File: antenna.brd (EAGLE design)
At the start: 98 x 98 mm, 4 parts, among them X1 BU-SMA-V

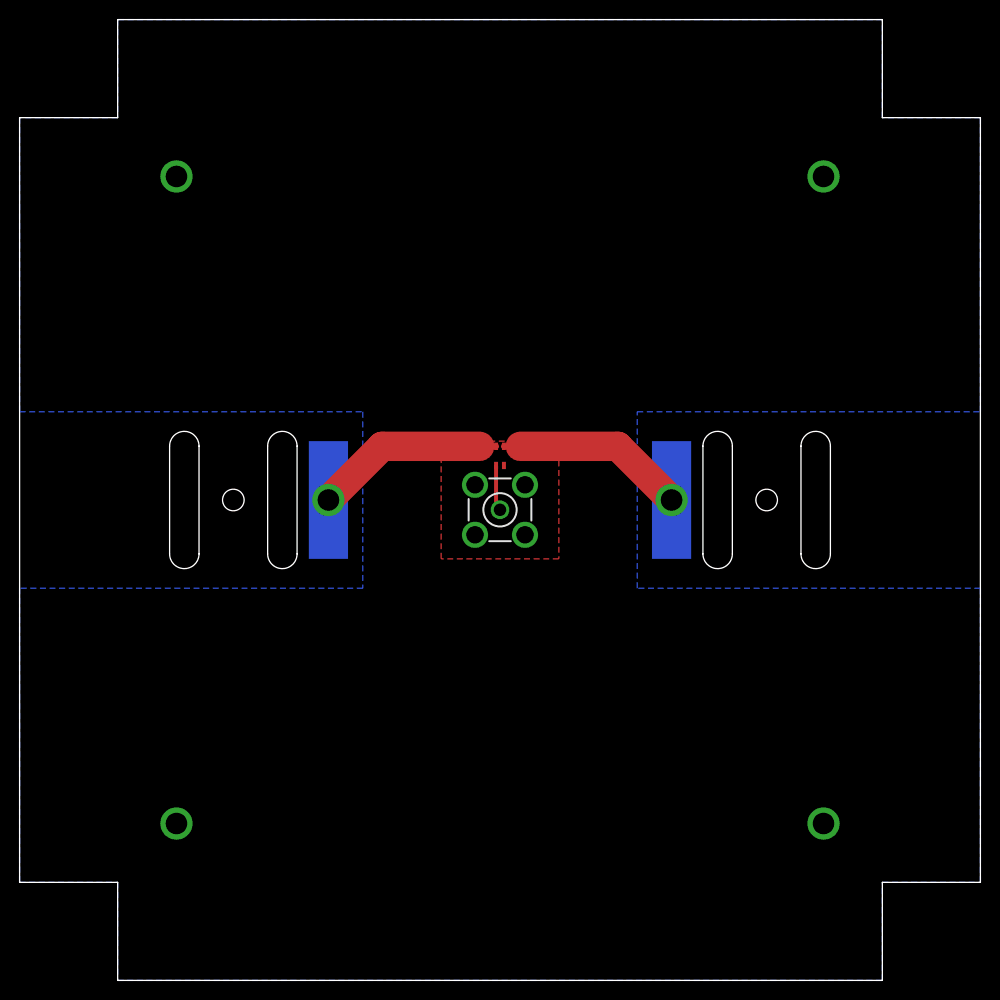
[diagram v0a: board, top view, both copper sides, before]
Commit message: Tweaks to antenna board
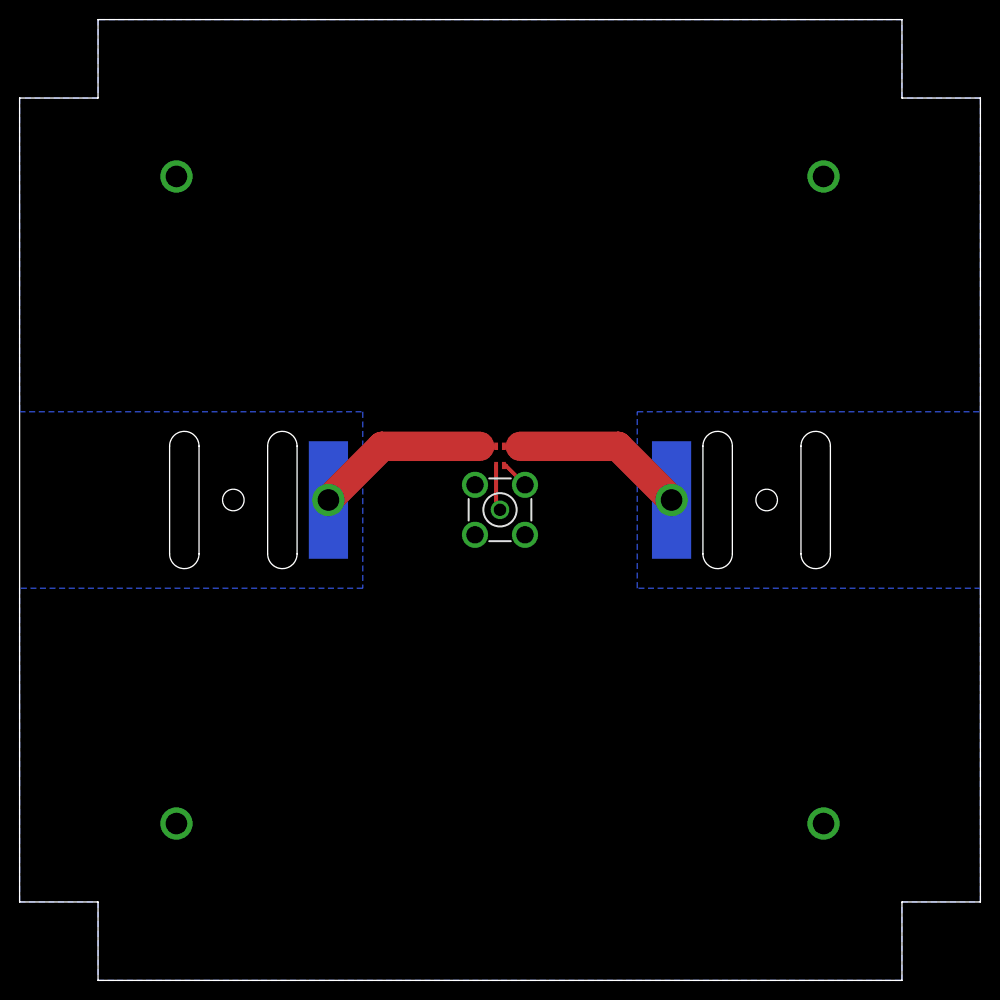
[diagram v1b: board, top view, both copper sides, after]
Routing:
- net GND: track 0.00 -> 2.97 mm
- removed copper zone on layer 1, net GND
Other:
- outline, holes or cut-outs redrawn
- board text added: "Antenna Board V1.1"
- board text removed: "Antenna Board V1.0"
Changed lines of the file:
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@@
 <board>
 <plain>
-<wire x1="0" y1="10" x2="10" y2="10" width="0" layer="20"/>
-<wire x1="10" y1="10" x2="10" y2="0" width="0" layer="20"/>
-<wire x1="10" y1="0" x2="88" y2="0" width="0" layer="20"/>
-<wire x1="88" y1="0" x2="88" y2="10" width="0" layer="20"/>
-<wire x1="88" y1="10" x2="98" y2="10" width="0" layer="20"/>
-<wire x1="98" y1="10" x2="98" y2="88" width="0" layer="20"/>
-<wire x1="98" y1="88" x2="88" y2="88" width="0" layer="20"/>
-<wire x1="88" y1="88" x2="88" y2="98" width="0" layer="20"/>
-<wire x1="88" y1="98" x2="10" y2="98" width="0" layer="20"/>
-<wire x1="10" y1="98" x2="10" y2="88" width="0" layer="20"/>
-<wire x1="10" y1="88" x2="0" y2="88" width="0" layer="20"/>
-<wire x1="0" y1="88" x2="0" y2="10" width="0" layer="20"/>
+<wire x1="0" y1="8" x2="8" y2="8" width="0" layer="20"/>
+<wire x1="8" y1="8" x2="8" y2="0" width="0" layer="20"/>
+<wire x1="8" y1="0" x2="90" y2="0" width="0" layer="20"/>
+<wire x1="90" y1="0" x2="90" y2="8" width="0" layer="20"/>
+<wire x1="90" y1="8" x2="98" y2="8" width="0" layer="20"/>
+<wire x1="98" y1="8" x2="98" y2="90" width="0" layer="20"/>
+<wire x1="98" y1="90" x2="90" y2="90" width="0" layer="20"/>
+<wire x1="90" y1="90" x2="90" y2="98" width="0" layer="20"/>
+<wire x1="90" y1="98" x2="8" y2="98" width="0" layer="20"/>
+<wire x1="8" y1="98" x2="8" y2="90" width="0" layer="20"/>
+<wire x1="8" y1="90" x2="0" y2="90" width="0" layer="20"/>
+<wire x1="0" y1="90" x2="0" y2="8" width="0" layer="20"/>
 <wire x1="82.7" y1="54.5" x2="82.7" y2="43.5" width="0" layer="20"/>
 <wire x1="79.7" y1="43.5" x2="79.7" y2="54.5" width="0" layer="20"/>
@@
 <rectangle x1="51.035" y1="30.205" x2="51.165" y2="30.215" layer="200"/>
 <rectangle x1="51.035" y1="30.215" x2="51.105" y2="30.225" layer="200"/>
-<text x="36.91" y="16.93" size="1.5" layer="200" font="vector">Antenna Board V1.0</text>
-<text x="37.25" y="78.82" size="1.5" layer="201" font="vector" rot="SMR180">Antenna Board V1.0</text>
+<text x="36.91" y="16.93" size="1.5" layer="200" font="vector">Antenna Board V1.1</text>
+<text x="37.25" y="78.82" size="1.5" layer="201" font="vector" rot="SMR180">Antenna Board V1.1</text>
 <rectangle x1="57.875" y1="75.465" x2="57.915" y2="75.475" layer="201"/>
 <rectangle x1="57.835" y1="75.455" x2="57.975" y2="75.465" layer="201"/>
@@
 <contactref element="X1" pad="4"/>
 <contactref element="X1" pad="5"/>
-<polygon width="0.4064" layer="1">
-<vertex x="43" y="55"/>
-<vertex x="55" y="55"/>
-<vertex x="55" y="43"/>
-<vertex x="43" y="43"/>
-</polygon>
 <via x="16" y="82" extent="1-16" drill="2.2"/>
 <via x="82" y="82" extent="1-16" drill="2.2"/>
@@
 <vertex x="35" y="40"/>
 <vertex x="0" y="40"/>
-<vertex x="0" y="10"/>
-<vertex x="10" y="10"/>
-<vertex x="10" y="0"/>
-<vertex x="88" y="0"/>
-<vertex x="88" y="10"/>
-<vertex x="98" y="10"/>
+<vertex x="0" y="8"/>
+<vertex x="8" y="8"/>
+<vertex x="8" y="0"/>
+<vertex x="90" y="0"/>
+<vertex x="90" y="8"/>
+<vertex x="98" y="8"/>
 <vertex x="98" y="40"/>
 <vertex x="63" y="40"/>
 <vertex x="63" y="58"/>
 <vertex x="98" y="58"/>
-<vertex x="98" y="88"/>
-<vertex x="88" y="88"/>
-<vertex x="88" y="98"/>
-<vertex x="10" y="98"/>
-<vertex x="10" y="88"/>
-<vertex x="0" y="88"/>
+<vertex x="98" y="90"/>
+<vertex x="90" y="90"/>
+<vertex x="90" y="98"/>
+<vertex x="8" y="98"/>
+<vertex x="8" y="90"/>
+<vertex x="0" y="90"/>
 </polygon>
+<wire x1="49.4" y1="52.525" x2="49.5748" y2="52.525" width="0.4064" layer="1"/>
+<wire x1="49.5748" y1="52.525" x2="51.5499" y2="50.5499" width="0.4064" layer="1"/>
 </signal>
 <signal name="N$2">
@@
 <contactref element="U$1" pad="P$1"/>
 <contactref element="U$1" pad="P$2"/>
-<wire x1="48.6" y1="54.475" x2="46.925" y2="54.475" width="0.6096" layer="1"/>
+<wire x1="48.6" y1="54.475" x2="46.925" y2="54.475" width="0.4064" layer="1"/>
 <wire x1="46.925" y1="54.475" x2="36.975" y2="54.475" width="3" layer="1"/>
 <wire x1="36.975" y1="54.475" x2="31.5" y2="49" width="3" layer="1"/>
@@
 <contactref element="U$2" pad="P$1"/>
 <contactref element="U$2" pad="P$2"/>
-<wire x1="49.4" y1="54.475" x2="51.075" y2="54.475" width="0.6096" layer="1"/>
+<wire x1="49.4" y1="54.475" x2="51.075" y2="54.475" width="0.4064" layer="1"/>
 <wire x1="51.075" y1="54.475" x2="61.025" y2="54.475" width="3" layer="1"/>
 <wire x1="61.025" y1="54.475" x2="66.5" y2="49" width="3" layer="1"/>

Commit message: Switching to teensy for flight computer
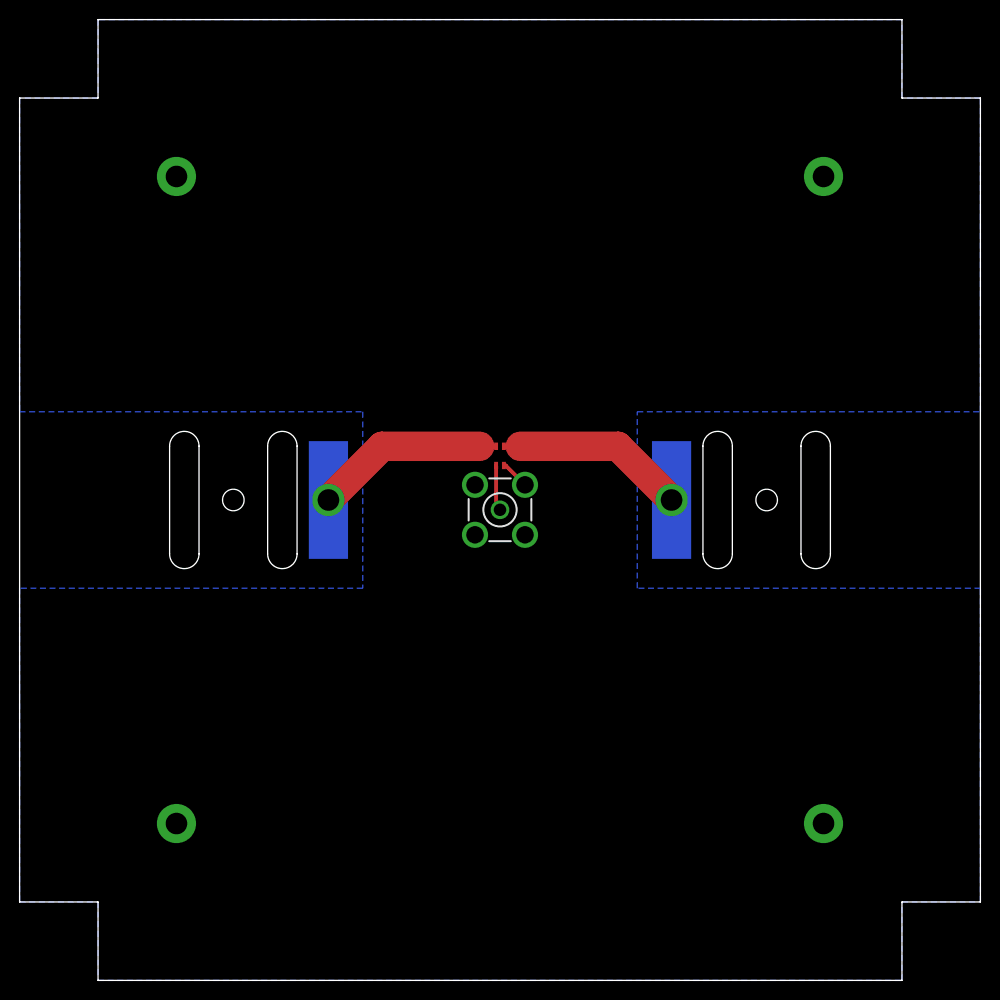
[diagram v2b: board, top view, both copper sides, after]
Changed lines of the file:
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@@
 <?xml version="1.0" encoding="utf-8"?>
 <!DOCTYPE eagle SYSTEM "eagle.dtd">
-<eagle version="6.5.0">
+<eagle version="6.6.0">
 <drawing>
 <settings>
@@
 <contactref element="X1" pad="4"/>
 <contactref element="X1" pad="5"/>
-<via x="16" y="82" extent="1-16" drill="2.2"/>
-<via x="82" y="82" extent="1-16" drill="2.2"/>
-<via x="16" y="16" extent="1-16" drill="2.2"/>
-<via x="82" y="16" extent="1-16" drill="2.2"/>
+<via x="16" y="82" extent="1-16" drill="2.2" diameter="4"/>
+<via x="82" y="82" extent="1-16" drill="2.2" diameter="4"/>
+<via x="16" y="16" extent="1-16" drill="2.2" diameter="4"/>
+<via x="82" y="16" extent="1-16" drill="2.2" diameter="4"/>
 <polygon width="0.4064" layer="16">
 <vertex x="0" y="58"/>

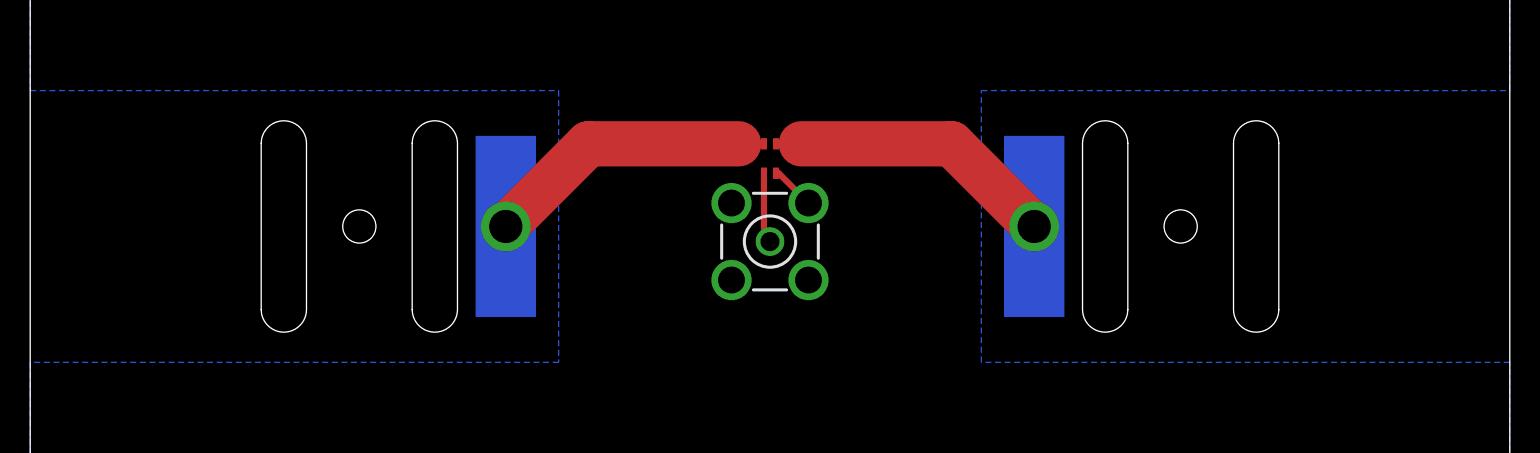
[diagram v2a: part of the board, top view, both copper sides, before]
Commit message: Increased size of tape antenna solder pads
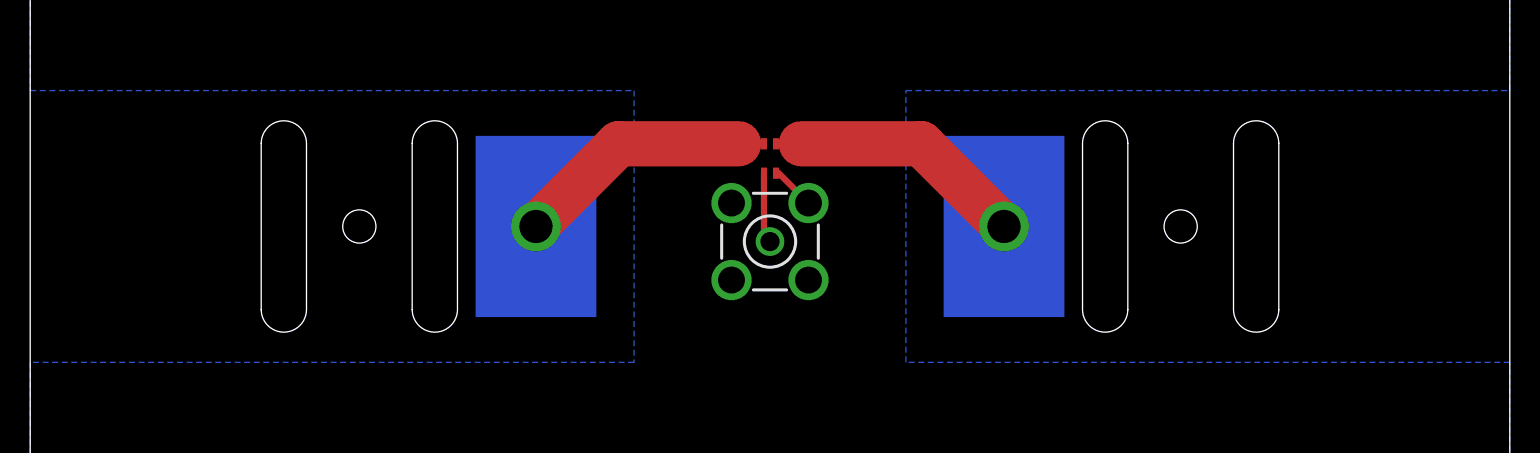
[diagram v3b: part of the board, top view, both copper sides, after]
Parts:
- moved U$1 2.00 mm to (33.5, 49.0)
- moved U$2 2.00 mm to (64.5, 49.0)
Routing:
- net N$3: track 19.4 -> 17.4 mm
- net N$2: track 19.4 -> 17.4 mm
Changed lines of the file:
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@@
 </element>
 <element name="B1" library="Balun" package="BALUN" value="BALUN" x="49" y="53.5" smashed="yes" rot="R90"/>
-<element name="U$1" library="TapeAntenna" package="TAPEANTENNA" value="TAPEANTENNA" x="31.5" y="49" rot="MR0"/>
-<element name="U$2" library="TapeAntenna" package="TAPEANTENNA" value="TAPEANTENNA" x="66.5" y="49" rot="MR0"/>
+<element name="U$1" library="TapeAntenna" package="TAPEANTENNA" value="TAPEANTENNA" x="33.5" y="49" rot="MR0"/>
+<element name="U$2" library="TapeAntenna" package="TAPEANTENNA" value="TAPEANTENNA" x="64.5" y="49" rot="MR0"/>
 </elements>
 <signals>
@@
 <polygon width="0.4064" layer="16">
 <vertex x="0" y="58"/>
-<vertex x="35" y="58"/>
-<vertex x="35" y="40"/>
+<vertex x="40" y="58"/>
+<vertex x="40" y="40"/>
 <vertex x="0" y="40"/>
 <vertex x="0" y="8"/>
@@
 <vertex x="98" y="8"/>
 <vertex x="98" y="40"/>
-<vertex x="63" y="40"/>
-<vertex x="63" y="58"/>
+<vertex x="58" y="40"/>
+<vertex x="58" y="58"/>
 <vertex x="98" y="58"/>
 <vertex x="98" y="90"/>
@@
 <contactref element="U$1" pad="P$2"/>
 <wire x1="48.6" y1="54.475" x2="46.925" y2="54.475" width="0.4064" layer="1"/>
-<wire x1="46.925" y1="54.475" x2="36.975" y2="54.475" width="3" layer="1"/>
-<wire x1="36.975" y1="54.475" x2="31.5" y2="49" width="3" layer="1"/>
+<wire x1="46.925" y1="54.475" x2="38.975" y2="54.475" width="3" layer="1"/>
+<wire x1="38.975" y1="54.475" x2="33.5" y2="49" width="3" layer="1"/>
 </signal>
 <signal name="N$3">
@@
 <contactref element="U$2" pad="P$2"/>
 <wire x1="49.4" y1="54.475" x2="51.075" y2="54.475" width="0.4064" layer="1"/>
-<wire x1="51.075" y1="54.475" x2="61.025" y2="54.475" width="3" layer="1"/>
-<wire x1="61.025" y1="54.475" x2="66.5" y2="49" width="3" layer="1"/>
+<wire x1="51.075" y1="54.475" x2="59.025" y2="54.475" width="3" layer="1"/>
+<wire x1="59.025" y1="54.475" x2="64.5" y2="49" width="3" layer="1"/>
 </signal>
 </signals>

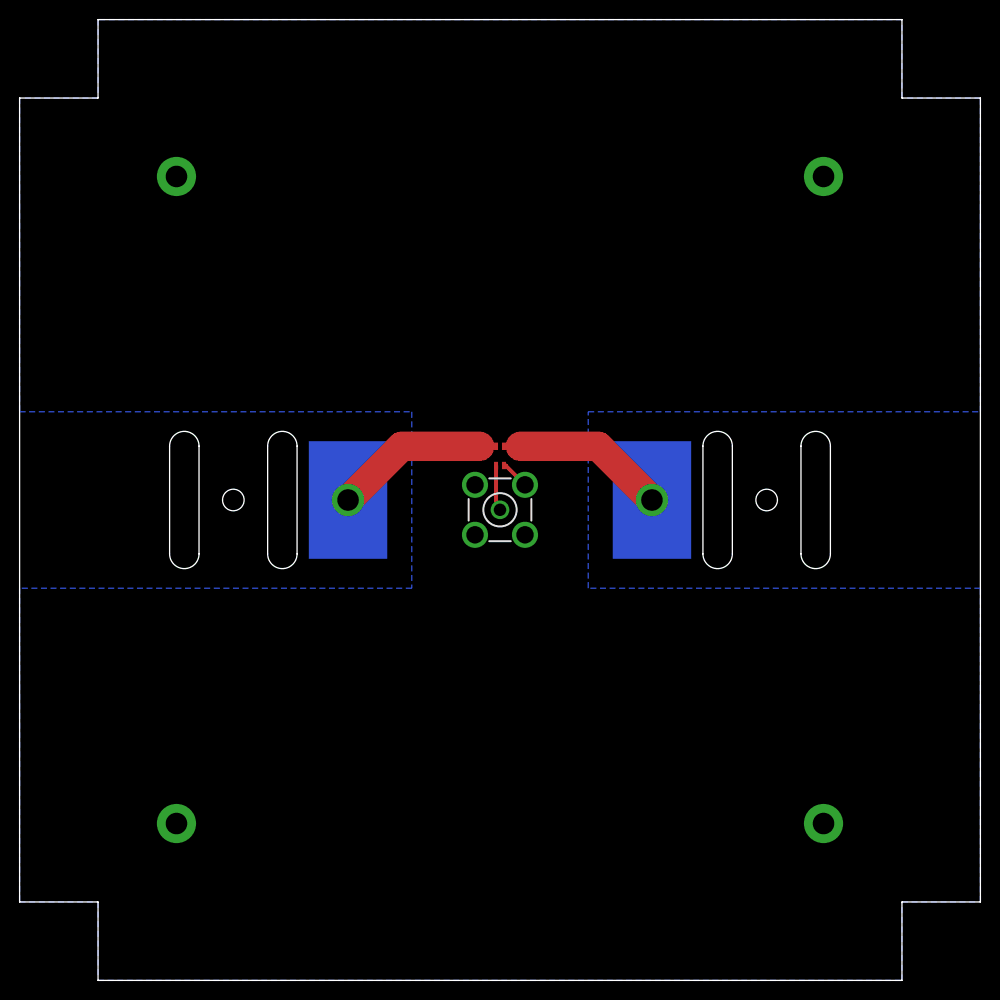
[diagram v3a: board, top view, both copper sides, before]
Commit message: Added solar cells to antenna board
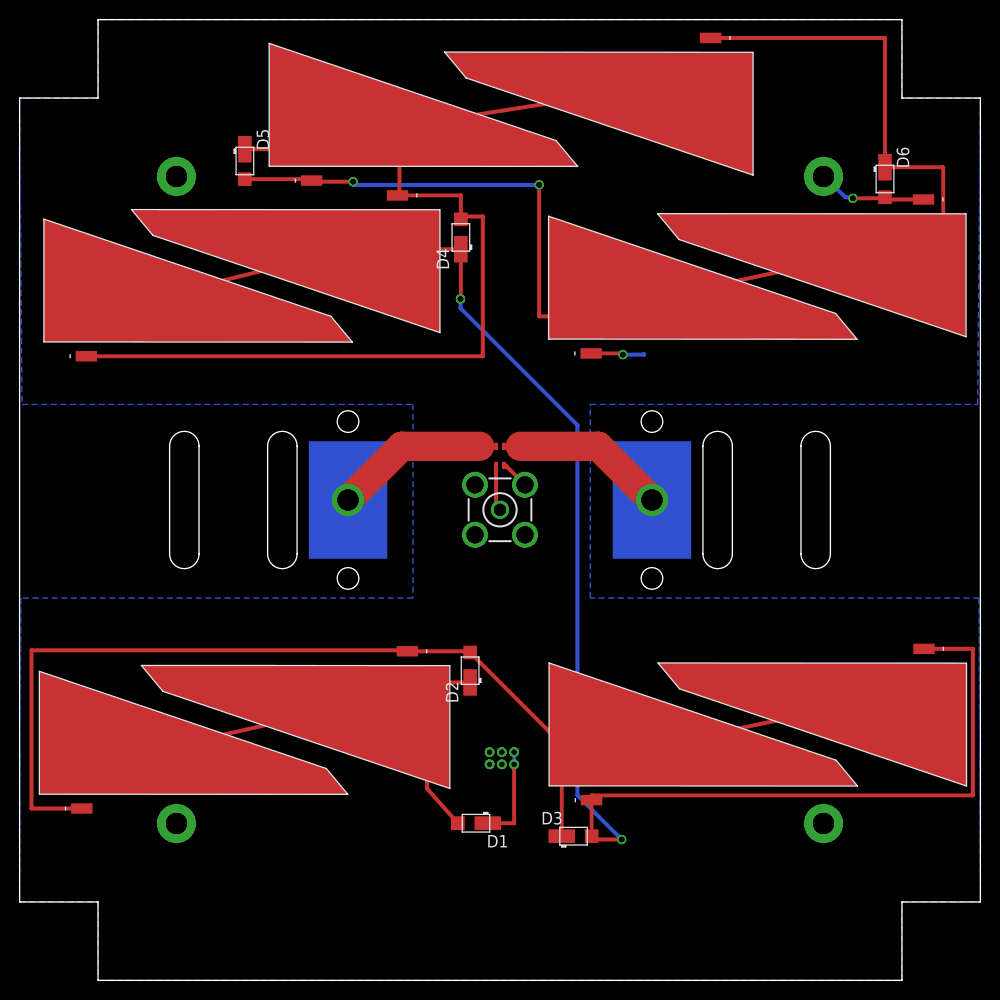
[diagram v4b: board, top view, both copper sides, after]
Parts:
- added D1, D2, D3, D4, D5, D6: SB_DIODE, phonesat:SB_DIODE
- added SL1, SL10, SL2, SL3, SL4, SL5, SL6, SL7, SL8, SL9: SOLAR_CELL, phonesat:SOLAR_CELL
- added U$4: G125-FV20605L0P, G125-FV20605L0P:G125-FV20605L0P
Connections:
- new net N$37: D3.POS, D4.NEG, SL3.1, SL4.1, SL5.2, SL6.2
- new net N$39: D4.POS, D5.NEG, SL5.1, SL6.1, SL7.2, SL8.2
- new net N$45: D2.POS, D3.NEG, SL1.1, SL2.1, SL3.2, SL4.2
- new net N$50: D5.POS, D6.NEG, SL10.2, SL7.1, SL8.1, SL9.2
- new net N$9: D1.POS, D2.NEG, SL1.2, SL2.2
- new net V_SOLAR: D1.NEG, U$4.P3, U$4.P6
- net GND: now also D6.POS, SL10.1, SL9.1, U$4.P1, U$4.P4
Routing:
- net N$37: track 0.00 -> 175.2 mm, vias 0 -> 2
- net N$50: track 0.00 -> 130.1 mm, vias 0 -> 2
- net N$45: track 0.00 -> 129.9 mm
- net N$39: track 0.00 -> 124.0 mm
- net N$9: track 0.00 -> 58.1 mm
- net GND: track 2.97 -> 20.4 mm, vias 4 -> 6
- net V_SOLAR: track 0.00 -> 9.94 mm
